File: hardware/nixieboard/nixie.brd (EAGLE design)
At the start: 104.4 x 64.1 mm, 60 parts

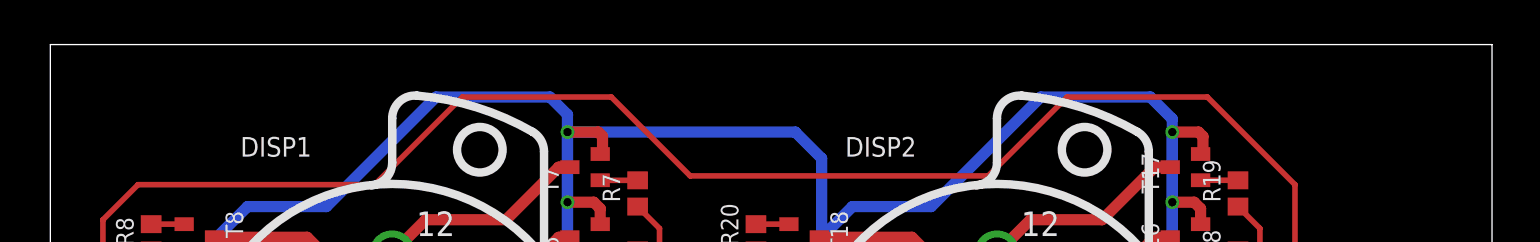
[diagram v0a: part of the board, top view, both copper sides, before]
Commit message: added connectors to nixieboard for stability
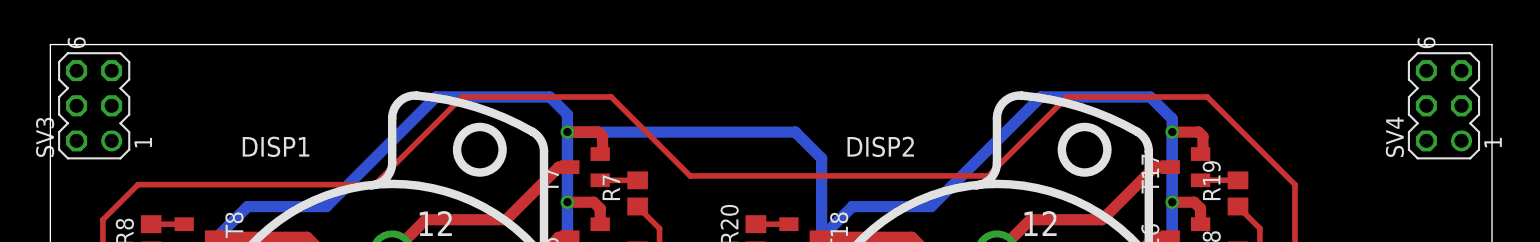
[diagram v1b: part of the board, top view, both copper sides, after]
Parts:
- added SV3, SV4: (no value), con-lstb:MA03-2
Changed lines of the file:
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@@
 <?xml version="1.0" encoding="utf-8"?>
 <!DOCTYPE eagle SYSTEM "eagle.dtd">
-<eagle version="7.2.0">
+<eagle version="6.5.0">
 <drawing>
 <settings>
@@
 <pass name="Default">
 <param name="RoutingGrid" value="50mil"/>
-<param name="AutoGrid" value="1"/>
-<param name="Efforts" value="0"/>
-<param name="TopRouterVariant" value="1"/>
 <param name="tpViaShape" value="round"/>
-<param name="PrefDir.1" value="a"/>
+<param name="PrefDir.1" value="|"/>
 <param name="PrefDir.2" value="0"/>
 <param name="PrefDir.3" value="0"/>
@@
 <param name="PrefDir.14" value="0"/>
 <param name="PrefDir.15" value="0"/>
-<param name="PrefDir.16" value="a"/>
+<param name="PrefDir.16" value="-"/>
 <param name="cfVia" value="8"/>
 <param name="cfNonPref" value="5"/>
@@
 <element name="SJ5" library="jumper" package="SJ" value="" x="24.13" y="12.7" rot="MR0"/>
 <element name="SJ6" library="jumper" package="SJ" value="" x="24.13" y="15.24" rot="MR0"/>
+<element name="SV3" library="con-lstb" package="MA03-2" value="" x="2.54" y="59.055" rot="R90">
+<attribute name="OC_NEWARK" value="unknown" x="2.54" y="59.055" size="1.778" layer="27" rot="R90" display="off"/>
+<attribute name="MPN" value="" x="2.54" y="59.055" size="1.778" layer="27" rot="R90" display="off"/>
+<attribute name="MF" value="" x="2.54" y="59.055" size="1.778" layer="27" rot="R90" display="off"/>
+<attribute name="OC_FARNELL" value="unknown" x="2.54" y="59.055" size="1.778" layer="27" rot="R90" display="off"/>
+</element>
+<element name="SV4" library="con-lstb" package="MA03-2" value="" x="100.33" y="59.055" rot="R90">
+<attribute name="OC_NEWARK" value="unknown" x="100.33" y="59.055" size="1.778" layer="27" rot="R90" display="off"/>
+<attribute name="MPN" value="" x="100.33" y="59.055" size="1.778" layer="27" rot="R90" display="off"/>
+<attribute name="MF" value="" x="100.33" y="59.055" size="1.778" layer="27" rot="R90" display="off"/>
+<attribute name="OC_FARNELL" value="unknown" x="100.33" y="59.055" size="1.778" layer="27" rot="R90" display="off"/>
+</element>
 </elements>
 <signals>

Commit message: added clock dots
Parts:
- added R25, R26, R27, R28: (no value), resistor:R0805
- added SG1, SG2: F/CM12P, buzzer:F/CM12P
- added T21, T22: (no value), transistor:SOT23-BEC
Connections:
- new net DOT1: SG1.-, T21.C
- new net DOT2: SG2.-, T22.C
- new net DOTS: R27.1, R28.1, U$2.16
- new net N$28: R25.1, SG1.+
- new net N$29: R26.1, SG2.+
- new net N$30: R27.2, T21.B
- new net N$31: R28.2, T22.B
- net GND: now also T21.E, T22.E
- net HV: now also R25.2, R26.2
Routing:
- net DOTS: track 0.00 -> 74.4 mm, vias 0 -> 5
- net GND: track 433.4 -> 459.6 mm, vias 25 -> 27
- net HV: track 119.5 -> 142.0 mm
- net DOT1: track 0.00 -> 11.4 mm
- net DOT2: track 0.00 -> 10.7 mm
- net N$28: track 0.00 -> 4.13 mm
- net N$29: track 0.00 -> 3.31 mm
- net N$31: track 0.00 -> 2.29 mm
- net N$30: track 0.00 -> 2.29 mm
- net VCC_MC: track 146.0 -> 148.1 mm
- net 2MC_K9: track 44.0 -> 45.1 mm
- net SDA: track 112.7 -> 113.8 mm
- net SCL: track 108.5 -> 109.2 mm
- net 2MC_K8: track 78.1 -> 77.5 mm

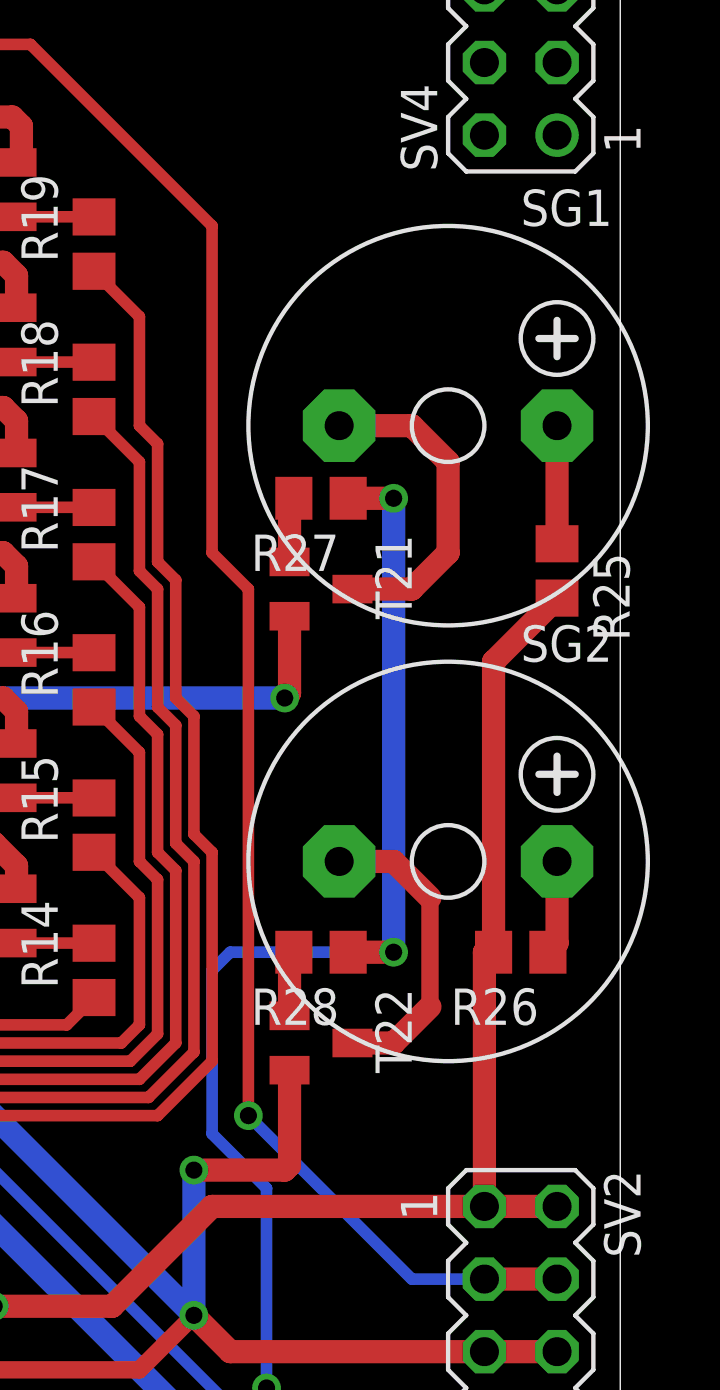
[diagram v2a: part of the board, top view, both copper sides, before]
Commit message: fixed dot distances
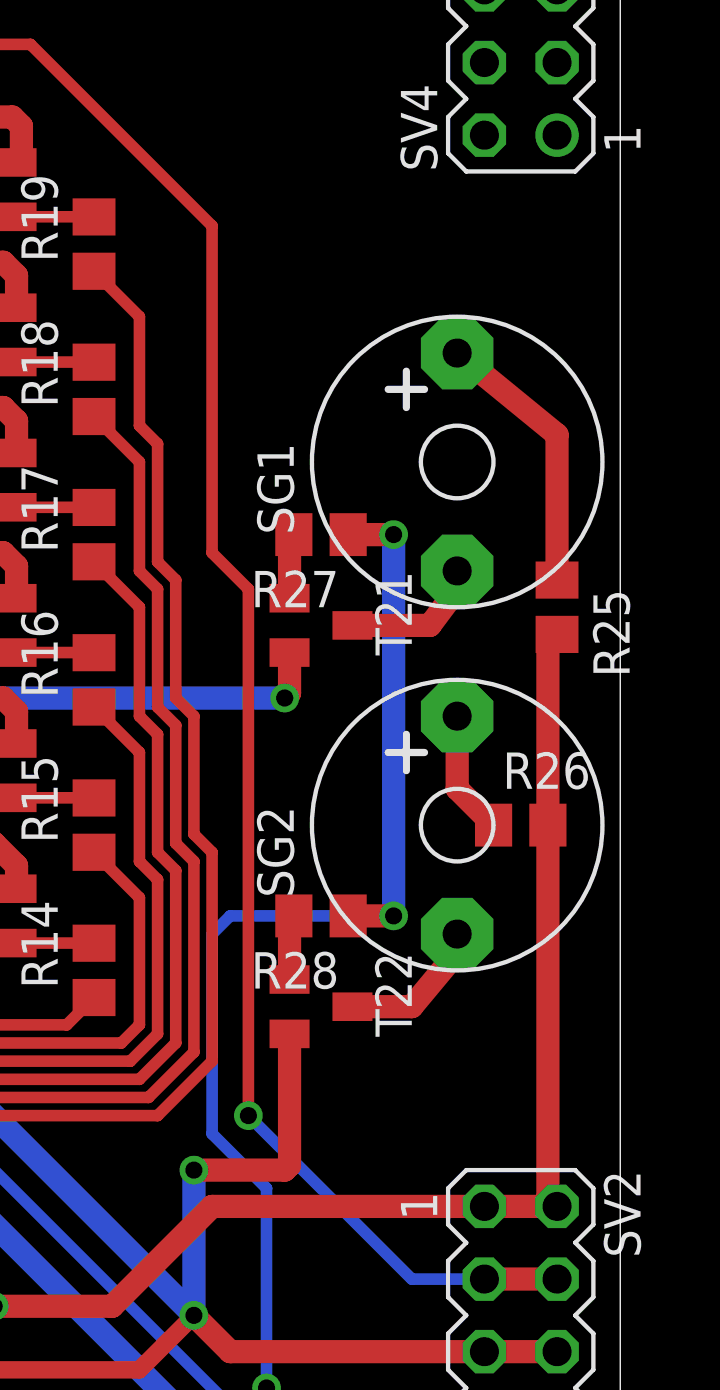
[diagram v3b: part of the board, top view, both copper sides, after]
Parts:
- SG1, SG2: device buzzer:F/CM12P -> ins1:F/CM12P
- moved R26 4.44 mm to (100.3, 32.4), turned to 0 degrees
- moved SG2 1.31 mm to (98.1, 32.4), turned to 90 degrees
- moved SG1 1.31 mm to (98.1, 45.1), turned to 90 degrees
- moved T21 1.27 mm to (93.3, 39.4)
- moved R28 1.27 mm to (93.3, 29.2)
- moved T22 1.27 mm to (93.3, 26.0)
- moved R25 1.27 mm to (101.6, 40.0)
- moved R27 1.27 mm to (93.3, 42.5)
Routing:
- net DOT1: track 11.4 -> 4.93 mm
- net DOT2: track 10.7 -> 5.19 mm
- net N$28: track 4.13 -> 9.60 mm
- net HV: track 142.0 -> 139.8 mm
- net DOTS: track 74.4 -> 73.1 mm
- net N$29: track 3.31 -> 4.34 mm

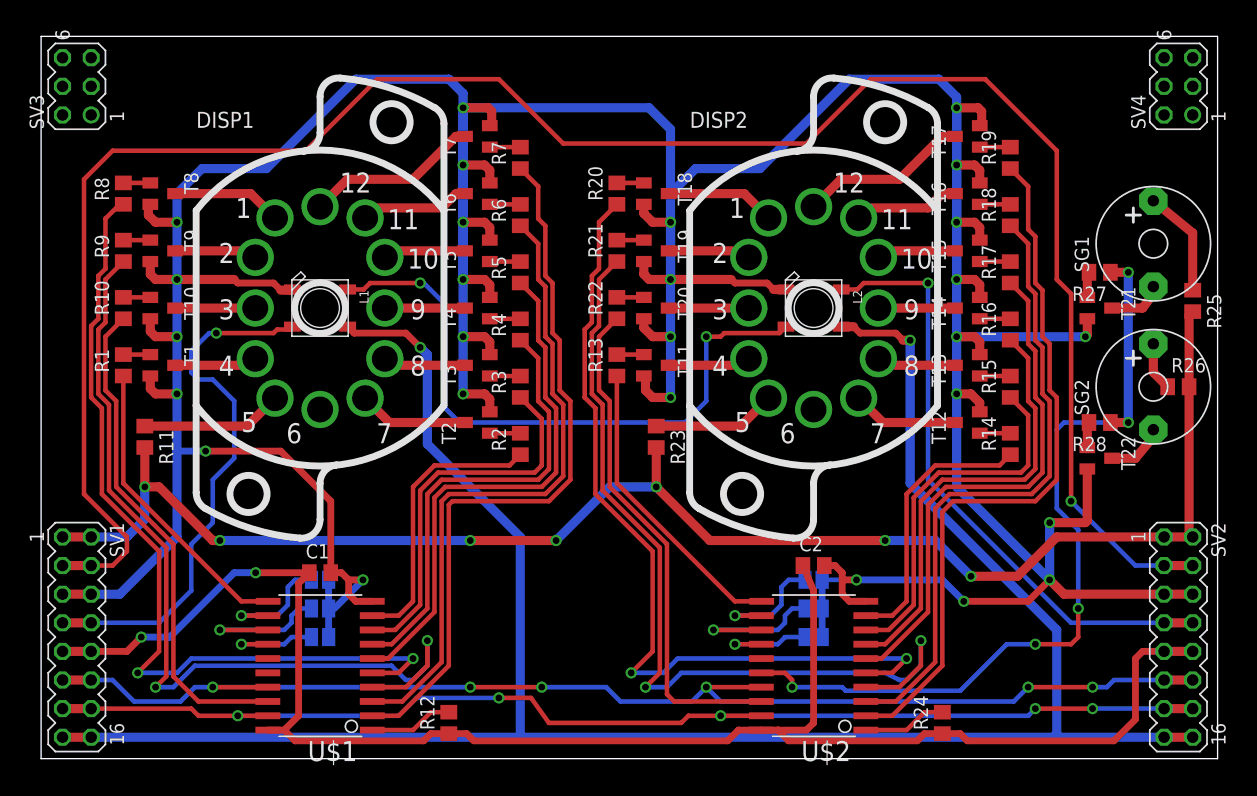
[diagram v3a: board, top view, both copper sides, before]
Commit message: fix DP IN-12A Pinout
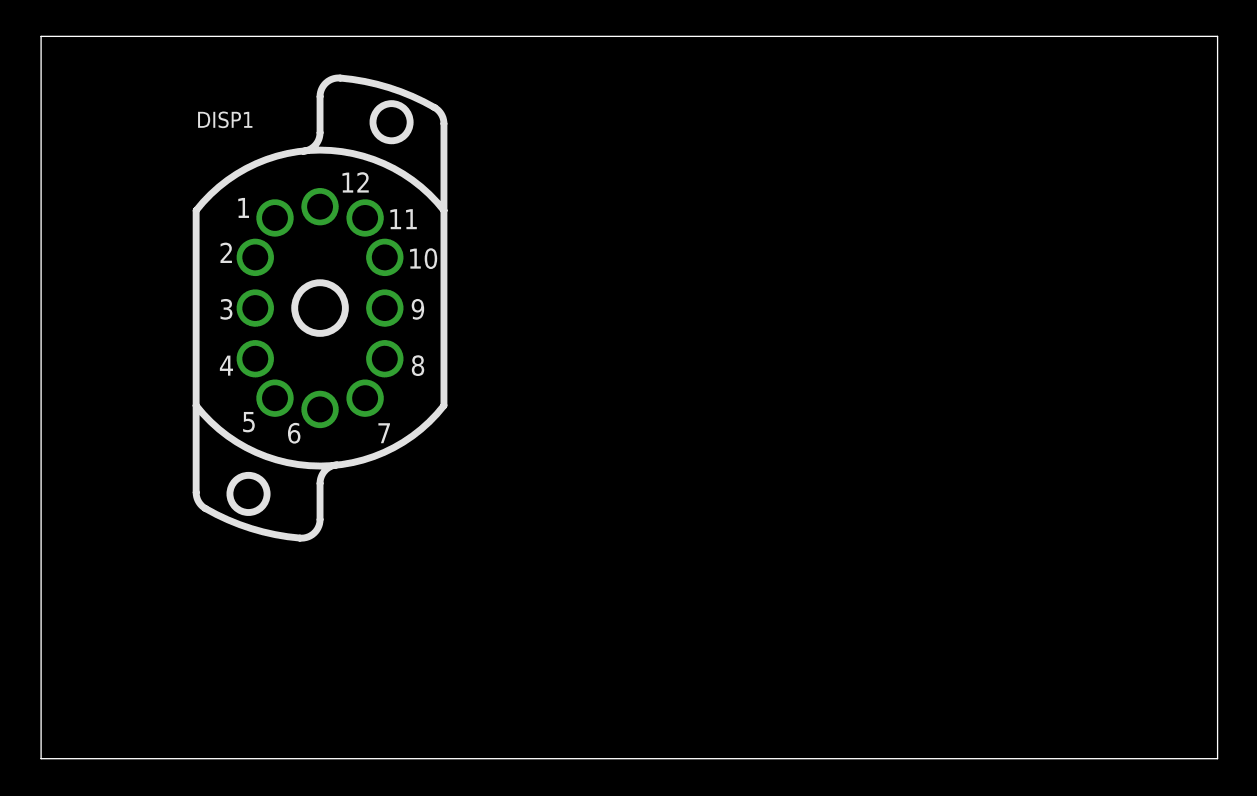
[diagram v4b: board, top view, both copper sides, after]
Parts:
- removed C1, C2: 100n, rcl:C0805
- removed DISP2: DISP_IN12A, dp_devices:DISP_IN-12_SOCKET
- removed L1, L2: WS2812B, adafruit:WS2812B
- removed R1, R10, R11, R12, R13, R14, R15, R16, R17, R18, R19, R2, R20, R21, R22, R23, R24, R25, R26, R27, R28, R3, R4, R5, R6, R7, R8, R9: (no value), resistor:R0805
- removed SG1, SG2: F/CM12P, ins1:F/CM12P
- removed SJ1, SJ2, SJ3, SJ4, SJ5, SJ6: (no value), jumper:SJ
- removed SV1, SV2: (no value), con-lstb:MA08-2
- removed SV3, SV4: (no value), con-lstb:MA03-2
- removed T1, T10, T11, T12, T13, T14, T15, T16, T17, T18, T19, T2, T20, T21, T22, T3, T4, T5, T6, T7, T8, T9: (no value), transistor:SOT23-BEC
- removed U$1, U$2: TINY2313-*S*, avr-6:SO20L$
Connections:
- removed net 1K0: DISP1.2, T1.C
- removed net 1K1: DISP1.11, T2.C
- removed net 1K2: DISP1.10, T3.C
- removed net 1K3: DISP1.9, T4.C
- removed net 1K4: DISP1.8, T5.C
- removed net 1K5: DISP1.7, T6.C
- removed net 1K6: DISP1.6, T7.C
- removed net 1K7: DISP1.5, T8.C
- removed net 1K8: DISP1.4, T9.C
- removed net 1K9: DISP1.3, T10.C
- removed net 1MC_K0: R1.1, U$1.11
- removed net 1MC_K1: R2.1, U$1.9
- removed net 1MC_K2: R3.1, U$1.8
- removed net 1MC_K3: R4.1, U$1.7
- removed net 1MC_K4: R5.1, U$1.6
- removed net 1MC_K5: R6.1, U$1.3
- removed net 1MC_K6: R7.1, U$1.2
- removed net 1MC_K7: R8.1, U$1.5
- removed net 1MC_K8: R9.1, U$1.4
- removed net 1MC_K9: R10.1, U$1.18
- removed net 2K0: DISP2.2, T11.C
- removed net 2K1: DISP2.11, T12.C
- removed net 2K2: DISP2.10, T13.C
- removed net 2K3: DISP2.9, T14.C
- removed net 2K4: DISP2.8, T15.C
- removed net 2K5: DISP2.7, T16.C
- removed net 2K6: DISP2.6, T17.C
- removed net 2K7: DISP2.5, T18.C
- removed net 2K8: DISP2.4, T19.C
- removed net 2K9: DISP2.3, T20.C
- removed net 2MC_K0: R13.1, U$2.11
- removed net 2MC_K1: R14.1, U$2.9
- removed net 2MC_K2: R15.1, U$2.8
- removed net 2MC_K3: R16.1, U$2.7
- removed net 2MC_K4: R17.1, U$2.6
- removed net 2MC_K5: R18.1, U$2.3
- removed net 2MC_K6: R19.1, U$2.2
- removed net 2MC_K7: R20.1, U$2.5
- removed net 2MC_K8: R21.1, U$2.4
- removed net 2MC_K9: R22.1, U$2.18
- removed net DOT1: SG1.-, T21.C
- removed net DOT2: SG2.-, T22.C
- removed net DOTS: R27.1, R28.1, U$2.16
- removed net GND: C1.2, C2.2, L1.3-GND, L2.3-GND, SJ1.1, SJ2.1, SJ3.1, SJ4.1, SJ5.1, SJ6.1, SV1.5, SV1.6, SV2.5, SV2.6, T1.E, T10.E, T11.E, T12.E, T13.E, T14.E, T15.E, T16.E, T17.E, T18.E, T19.E, T2.E, T20.E, T21.E, T22.E, T3.E, T4.E, T5.E, T6.E, T7.E, T8.E, T9.E, U$1.10, U$2.10
- removed net HV: R11.2, R23.2, R25.2, R26.2, SV1.1, SV1.2, SV2.1, SV2.2
- removed net HV_EN: SV1.3, SV1.4, SV2.3, SV2.4
- removed net I2C1_ADD0: SJ6.2, U$1.12
- removed net I2C1_ADD1: SJ5.2, U$1.13
- removed net I2C1_ADD2: SJ4.2, U$1.14
- removed net I2C2_ADD0: SJ3.2, U$2.12
- removed net I2C2_ADD1: SJ2.2, U$2.13
- removed net I2C2_ADD2: SJ1.2, U$2.14
- removed net N$1: R2.2, T2.B
- removed net N$10: R1.2, T1.B
- removed net N$11: DISP1.1, R11.1
- removed net N$12: R13.2, T11.B
- removed net N$13: R12.2, U$1.1
- removed net N$14: R14.2, T12.B
- removed net N$15: R15.2, T13.B
- removed net N$16: R16.2, T14.B
- removed net N$17: R17.2, T15.B
- removed net N$18: R18.2, T16.B
- removed net N$19: R19.2, T17.B
- removed net N$2: R3.2, T3.B
- removed net N$20: R20.2, T18.B
- removed net N$21: R21.2, T19.B
- removed net N$22: R22.2, T20.B
- removed net N$23: R24.2, U$2.1
- removed net N$24: DISP2.1, R23.1
- removed net N$25: L1.2-DOUT, L2.4-DIN
- removed net N$28: R25.1, SG1.+
- removed net N$29: R26.1, SG2.+
- removed net N$3: R4.2, T4.B
- removed net N$30: R27.2, T21.B
- removed net N$31: R28.2, T22.B
- removed net N$4: R5.2, T5.B
- removed net N$5: R6.2, T6.B
- removed net N$6: R7.2, T7.B
- removed net N$7: R8.2, T8.B
- removed net N$8: R9.2, T9.B
- removed net N$9: R10.2, T10.B
- removed net SCL: SV1.13, SV1.14, SV2.13, SV2.14, U$1.19, U$2.19
- removed net SDA: SV1.11, SV1.12, SV2.11, SV2.12, U$1.17, U$2.17
- removed net VCC_MC: C1.1, C2.1, R12.1, R24.1, SV1.10, SV1.9, SV2.10, SV2.9, U$1.20, U$2.20
- removed net VCC_WS: L1.1-VDD, L2.1-VDD, SV1.15, SV1.16, SV2.15, SV2.16
- removed net WS_IN: L1.4-DIN, SV1.7, SV1.8
- removed net WS_OUT: L2.2-DOUT, SV2.7, SV2.8
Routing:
- net GND: track 459.6 -> 0.00 mm, vias 27 -> 0
- net VCC_WS: track 193.2 -> 0.00 mm, vias 2 -> 0
- net HV_EN: track 183.0 -> 0.00 mm, vias 1 -> 0
- net VCC_MC: track 148.1 -> 0.00 mm, vias 2 -> 0
- net HV: track 139.8 -> 0.00 mm, vias 7 -> 0
- net SDA: track 113.8 -> 0.00 mm, vias 6 -> 0
- net SCL: track 109.2 -> 0.00 mm, vias 5 -> 0
- net 1MC_K8: track 77.7 -> 0.00 mm, vias 2 -> 0
- net 2MC_K8: track 77.5 -> 0.00 mm, vias 2 -> 0
- net 1MC_K7: track 75.4 -> 0.00 mm, vias 2 -> 0
- net 2MC_K7: track 75.2 -> 0.00 mm, vias 2 -> 0
- net DOTS: track 73.1 -> 0.00 mm, vias 5 -> 0
- net 1MC_K6: track 64.1 -> 0.00 mm
- net 2MC_K6: track 63.0 -> 0.00 mm
- net 1MC_K5: track 57.4 -> 0.00 mm
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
